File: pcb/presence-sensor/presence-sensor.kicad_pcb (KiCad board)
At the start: 4 copper layers, 30 x 36 mm, 35 parts, among them J1 Conn_Coaxial, J2 Conn_01x03_MountingPin, J3 USB_C_Receptacle_USB2.0_16P, SW1 SW_Push, SW2 SW_Push, U1 CC2340R52E0RGER, U2 SEN0609, U3 XC6206P332MR-G, Y1 48M, Y2 32k768

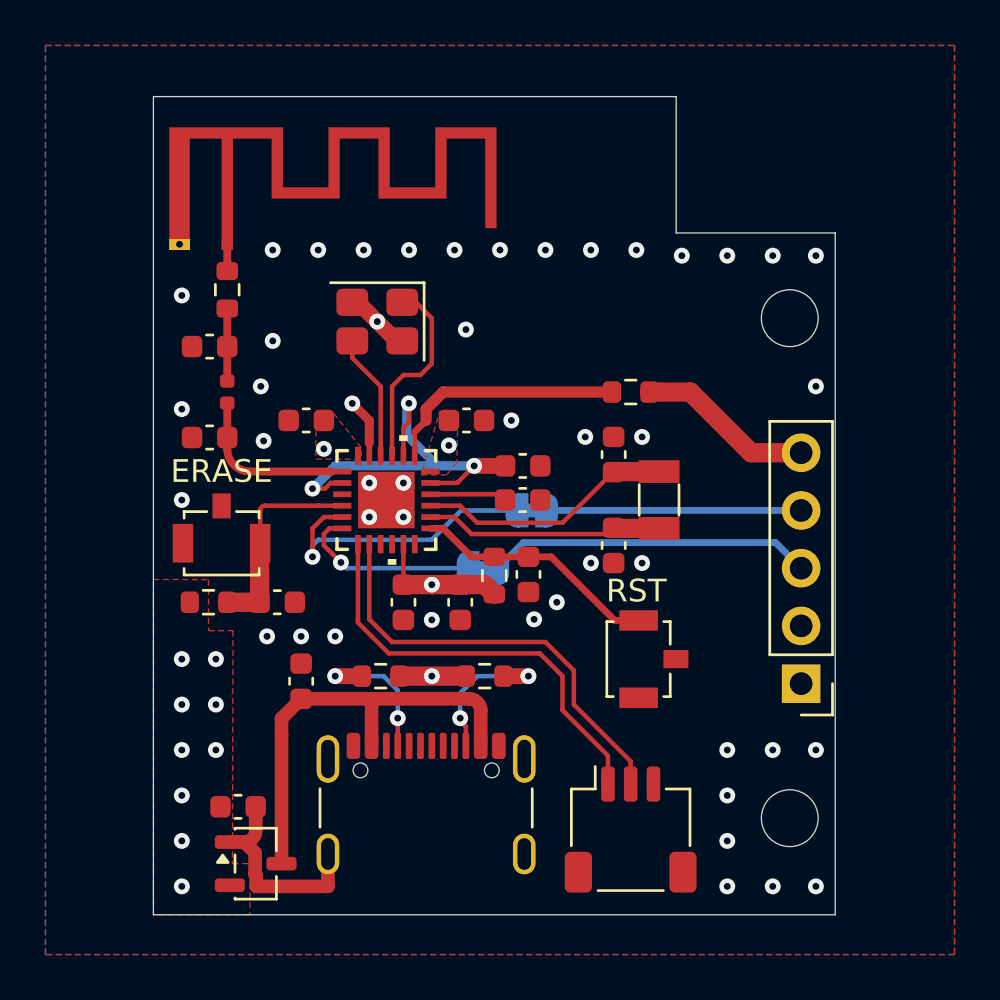
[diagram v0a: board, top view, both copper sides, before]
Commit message: rework VDDR and ERASE button
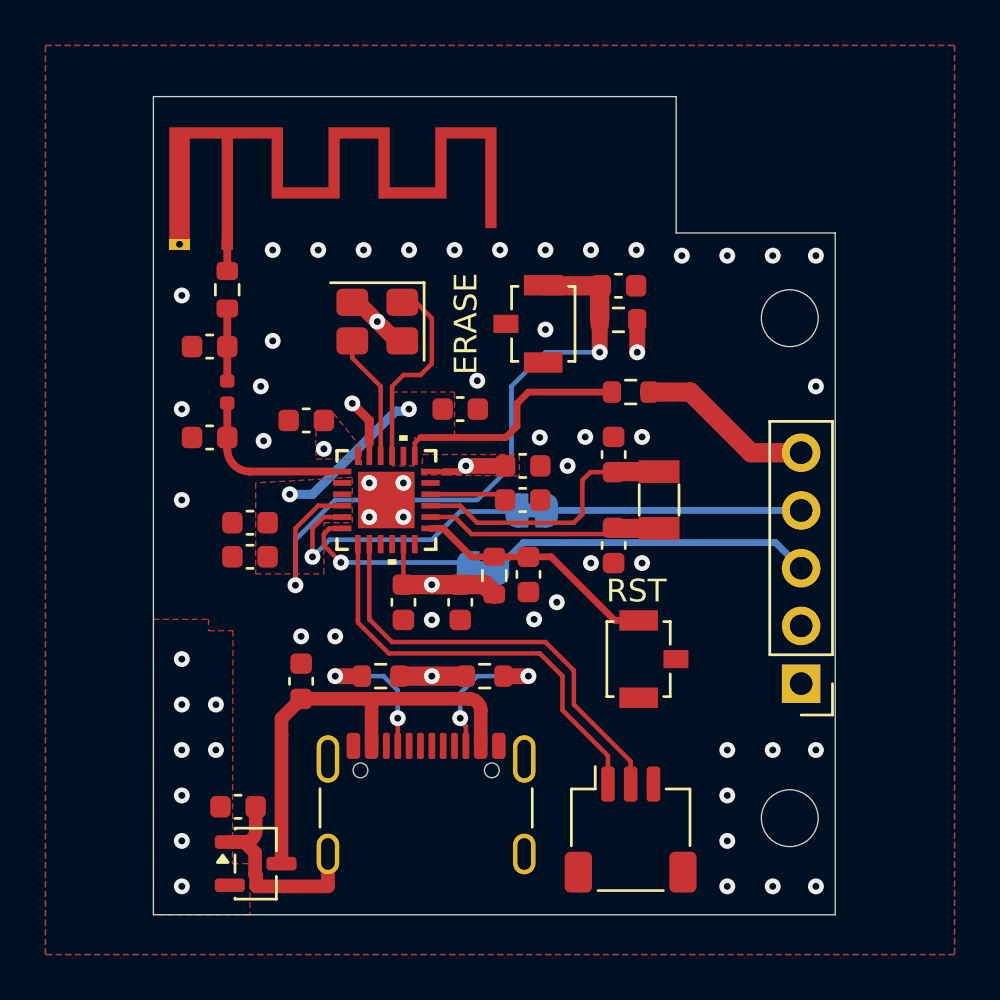
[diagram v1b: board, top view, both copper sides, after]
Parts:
- added C5: 0u1, Capacitor_SMD:C_0603_1608Metric, F.Cu at (143.2, 100.8)
- added C6: 0u1, Capacitor_SMD:C_0603_1608Metric, F.Cu at (152.5, 95.8)
- J2: value Conn_01x03_MountingPin -> RPI_DEBUG_PROBE
- moved R5 21.9 mm to (159.5, 91.8), turned to 0 degrees
- moved C17 20.5 mm to (159.5, 90.3)
- moved SW2 16.0 mm to (155.3, 92.0), turned to -90 degrees
- moved C10 12.6 mm to (143.2, 102.2), turned to 180 degrees
- moved C3 3.18 mm to (155.2, 98.2)
- turned C7 to 0 degrees
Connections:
- net Net-(J2-Pin_1) renamed /SWDIO
- net Net-(J2-Pin_2) renamed /SWCLK
- C10 pad 1: /+VDDR -> +VDDR
- C7 pad 1: GND -> +VDDD
- C7 pad 2: Net-(U1-VDDD) -> GND
- U1 pad 16: Net-(U1-VDDD) -> +VDDD
- U1 pad 17: /+VDDR -> unconnected-(U1-DCDC-Pad17)
- U1 pad 2: /+VDDR -> +VDDR
- U1 pad 20: /+VDDR -> +VDDR
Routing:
- net /ERASE: track 9.20 -> 31.3 mm, vias 0 -> 2
- net /+VDDR: track 18.3 -> 0.00 mm, vias 3 -> 0
- net +VDDR: track 0.00 -> 6.79 mm, vias 0 -> 2
- net +3V3: track 5.96 -> 10.8 mm
- net Net-(U1-VDDD): track 3.39 -> 0.00 mm
- net +VDDD: track 0.00 -> 3.39 mm
- net Net-(U1-DIO4_X32N): track 11.3 -> 12.2 mm
- net GND: vias 47 -> 48
- added copper zone on F.Cu, net +VDDR
